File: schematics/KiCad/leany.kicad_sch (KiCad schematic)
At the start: 25 parts, among them J1 SWD, J2 SSD1306, SW1 BOOTMODE_SW, SW2 ZERO_BTN, SW3 HOLD_BTN, U1 LSM6DSO, U2 STM32F103C8Tx, U3 CH340C, Y1 8MHz

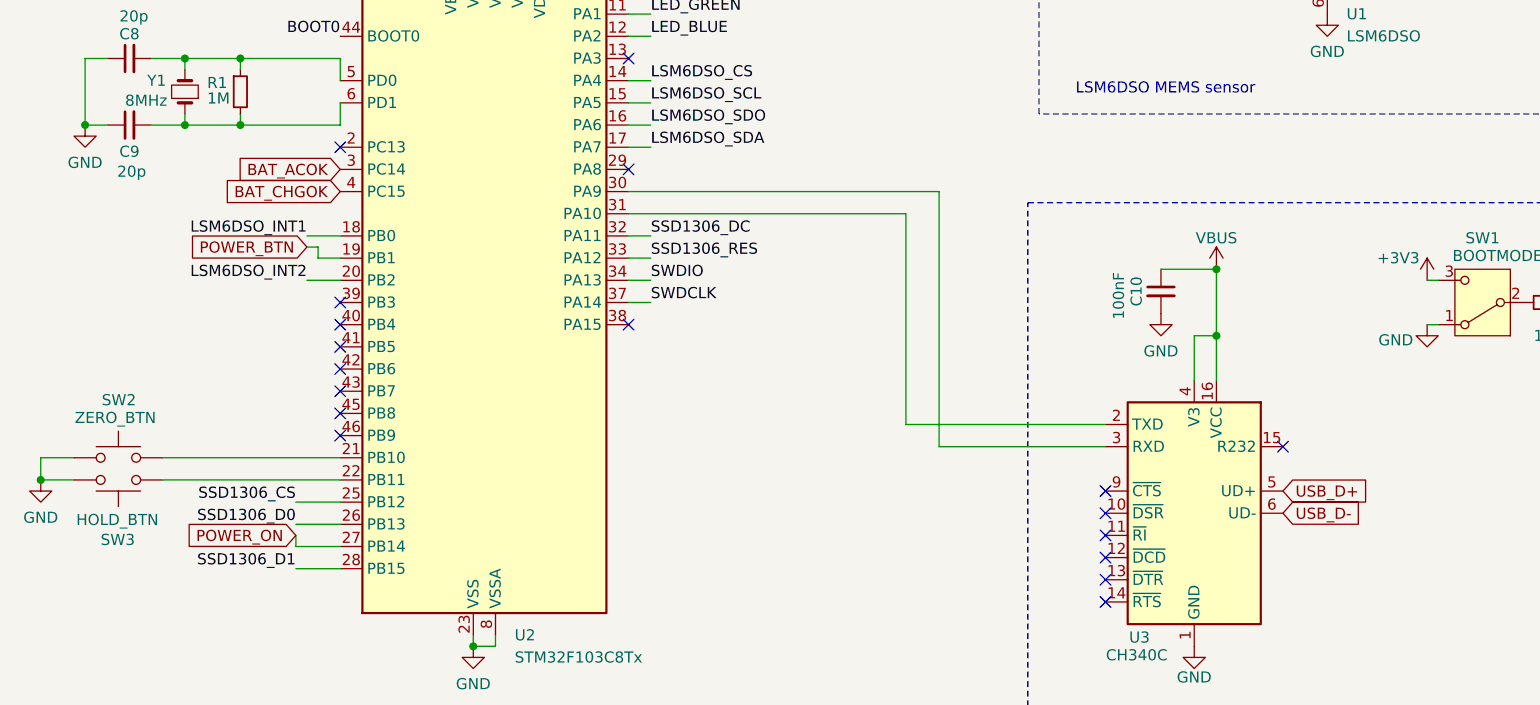
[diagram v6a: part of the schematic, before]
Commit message: add footprints and global labels directions
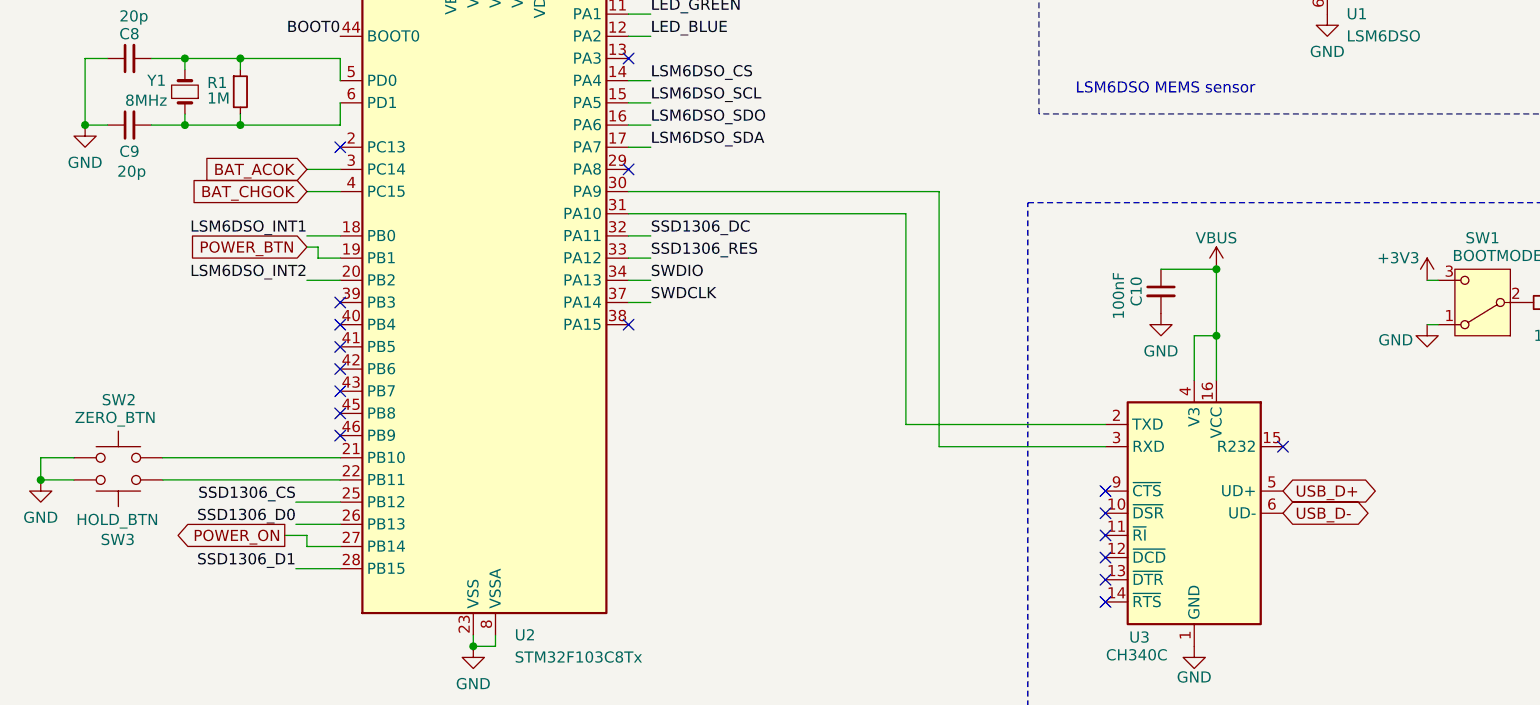
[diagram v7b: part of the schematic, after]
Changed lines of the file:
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@@
+	(wire
+		(pts
+			(xy 114.3 91.44) (xy 118.11 91.44)
+		)
+		(stroke
+			(width 0)
+			(type default)
+		)
+	)
 	(wire
 		(pts
@@
 	(wire
 		(pts
+			(xy 111.76 130.81) (xy 114.3 130.81)
+		)
+		(stroke
+			(width 0)
+			(type default)
+		)
+	)
+	(wire
+		(pts
 			(xy 157.48 50.8) (xy 157.48 49.53)
 		)
@@
 	(wire
 		(pts
+			(xy 114.3 130.81) (xy 114.3 132.08)
+		)
+		(stroke
+			(width 0)
+			(type default)
+		)
+	)
+	(wire
+		(pts
 			(xy 242.57 106.68) (xy 243.84 106.68)
 		)
@@
 	(wire
 		(pts
+			(xy 114.3 132.08) (xy 118.11 132.08)
+		)
+		(stroke
+			(width 0)
+			(type default)
+		)
+	)
+	(wire
+		(pts
 			(xy 133.35 46.99) (xy 133.35 49.53)
 		)
@@
 	(wire
 		(pts
-			(xy 113.03 130.81) (xy 113.03 132.08)
-		)
-		(stroke
-			(width 0)
-			(type default)
-		)
-	)
-	(wire
-		(pts
 			(xy 135.89 60.96) (xy 138.43 60.96)
 		)
@@
 	(wire
 		(pts
-			(xy 113.03 132.08) (xy 118.11 132.08)
-		)
-		(stroke
-			(width 0)
-			(type default)
-		)
-	)
-	(wire
-		(pts
 			(xy 153.67 68.58) (xy 151.13 68.58)
 		)
@@
 		(pts
 			(xy 163.83 49.53) (xy 157.48 49.53)
+		)
+		(stroke
+			(width 0)
+			(type default)
+		)
+	)
+	(wire
+		(pts
+			(xy 114.3 88.9) (xy 118.11 88.9)
 		)
 		(stroke
@@
 	(global_label "BAT_CHGOK"
 		(shape input)
-		(at 118.11 91.44 180)
+		(at 114.3 91.44 180)
 		(fields_autoplaced yes)
 		(effects
@@
 		)
 		(property "Intersheetrefs" "${INTERSHEET_REFS}"
-			(at 104.36 91.44 0)
+			(at 100.55 91.44 0)
 			(effects
 				(font
@@
 	(global_label "BAT_ACOK"
 		(shape input)
-		(at 118.11 88.9 180)
+		(at 114.3 88.9 180)
 		(fields_autoplaced yes)
 		(effects
@@
 		)
 		(property "Intersheetrefs" "${INTERSHEET_REFS}"
-			(at 105.8719 88.9 0)
+			(at 102.0619 88.9 0)
 			(effects
 				(font
@@
 	)
 	(global_label "USB_D+"
-		(shape input)
+		(shape bidirectional)
 		(at 226.06 125.73 0)
 		(fields_autoplaced yes)
@@
 		)
 		(property "Intersheetrefs" "${INTERSHEET_REFS}"
-			(at 236.6652 125.73 0)
+			(at 237.7765 125.73 0)
 			(effects
 				(font
@@
 	)
 	(global_label "USB_D-"
-		(shape input)
+		(shape bidirectional)
 		(at 226.06 128.27 0)
 		(fields_autoplaced yes)
@@
 		)
 		(property "Intersheetrefs" "${INTERSHEET_REFS}"
-			(at 236.6652 128.27 0)
+			(at 237.7765 128.27 0)
 			(effects
 				(font
@@
 	)
 	(global_label "POWER_ON"
-		(shape input)
-		(at 113.03 130.81 180)
+		(shape output)
+		(at 111.76 130.81 180)
 		(fields_autoplaced yes)
 		(effects
@@
 		)
 		(property "Intersheetrefs" "${INTERSHEET_REFS}"
-			(at 99.9453 130.81 0)
+			(at 98.6753 130.81 0)
 			(effects
 				(font

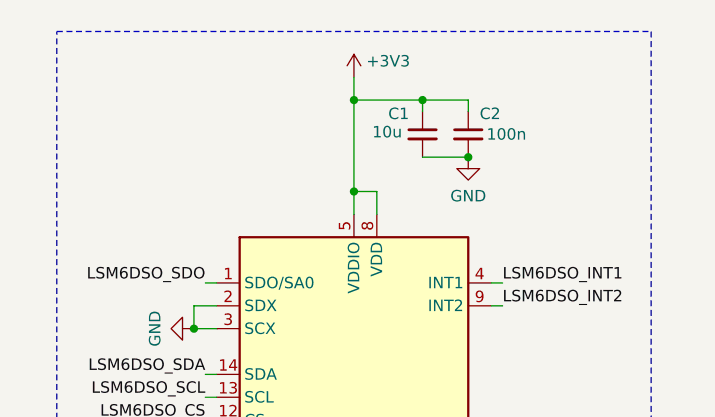
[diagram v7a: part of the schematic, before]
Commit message: replace 10uF capacitors by electrolytic ones
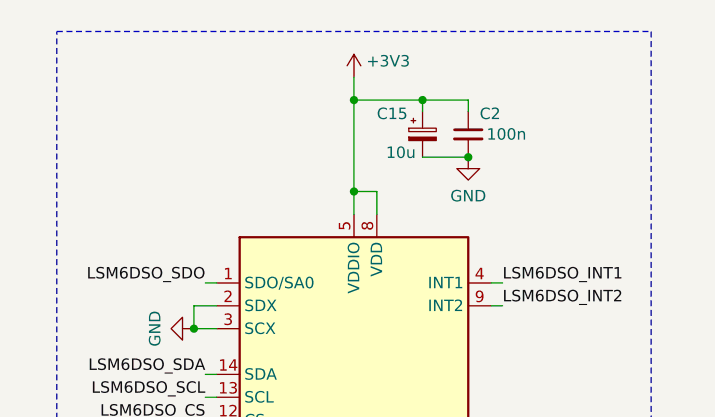
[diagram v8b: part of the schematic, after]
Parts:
- removed C1: 10u, Capacitor_SMD:C_0201_0603Metric, symbol Device:C_Small
- added C15: 10u, symbol Device:C_Polarized_Small
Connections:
- net +3V3: now also C15.1
- net GND: now also C15.2
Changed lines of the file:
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@@
-	)
-	(symbol
-		(lib_id "Device:C_Small")
-		(at 238.76 31.75 0)
-		(unit 1)
-		(exclude_from_sim no)
-		(in_bom yes)
-		(on_board yes)
-		(dnp no)
-		(property "Reference" "C1"
-			(at 234.95 29.464 0)
-			(effects
-				(font
-					(size 1.27 1.27)
-				)
-				(justify left)
-			)
-		)
-		(property "Value" "10u"
-			(at 233.172 31.496 0)
-			(effects
-				(font
-					(size 1.27 1.27)
-				)
-				(justify left)
-			)
-		)
-		(property "Footprint" "Capacitor_SMD:C_0201_0603Metric"
-			(at 238.76 31.75 0)
-			(effects
-				(font
-					(size 1.27 1.27)
-				)
-				(hide yes)
-			)
-		)
-		(property "Datasheet" "~"
-			(at 238.76 31.75 0)
-			(effects
-				(font
-					(size 1.27 1.27)
-				)
-				(hide yes)
-			)
-		)
-		(property "Description" "Unpolarized capacitor, small symbol"
-			(at 238.76 31.75 0)
-			(effects
-				(font
-					(size 1.27 1.27)
-				)
-				(hide yes)
-			)
-		)
-		(pin "2"
-		)
-		(pin "1"
-		)
-		(instances
-			(project "leany"
-				(path "/e47b2519-93ca-4a48-9414-ecc253dd35f5"
-					(reference "C1")
-					(unit 1)
-				)
-			)
-		)
 	)
 	(symbol
@@
 					(unit 1)
 				)
+			)
+		)
+	)
+	(symbol
+		(lib_id "Device:C_Polarized_Small")
+		(at 238.76 31.75 0)
+		(unit 1)
+		(exclude_from_sim no)
+		(in_bom yes)
+		(on_board yes)
+		(dnp no)
+		(property "Reference" "C15"
+			(at 233.68 29.464 0)
+			(effects
+				(font
+					(size 1.27 1.27)
+				)
+				(justify left)
+			)
+		)
+		(property "Value" "10u"
+			(at 234.696 33.782 0)
+			(effects
+				(font
+					(size 1.27 1.27)
+				)
+				(justify left)
+			)
+		)
+		(property "Footprint" ""
+			(at 238.76 31.75 0)
+			(effects
+				(font
+					(size 1.27 1.27)
+				)
+				(hide yes)
+			)
+		)
+		(property "Datasheet" "~"
+			(at 238.76 31.75 0)
+			(effects
+				(font
+					(size 1.27 1.27)
+				)
+				(hide yes)
+			)
+		)
+		(property "Description" "Polarized capacitor, small symbol"
+			(at 238.76 31.75 0)
+			(effects
+				(font
+					(size 1.27 1.27)
+				)
+				(hide yes)
+			)
+		)
+		(pin "1"
+		)
+		(pin "2"
+		)
+		(instances
+			(project "leany"
+				(path "/e47b2519-93ca-4a48-9414-ecc253dd35f5"
+					(reference "C15")
+					(unit 1)
+				)
